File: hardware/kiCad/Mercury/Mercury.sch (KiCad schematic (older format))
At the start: 55 parts

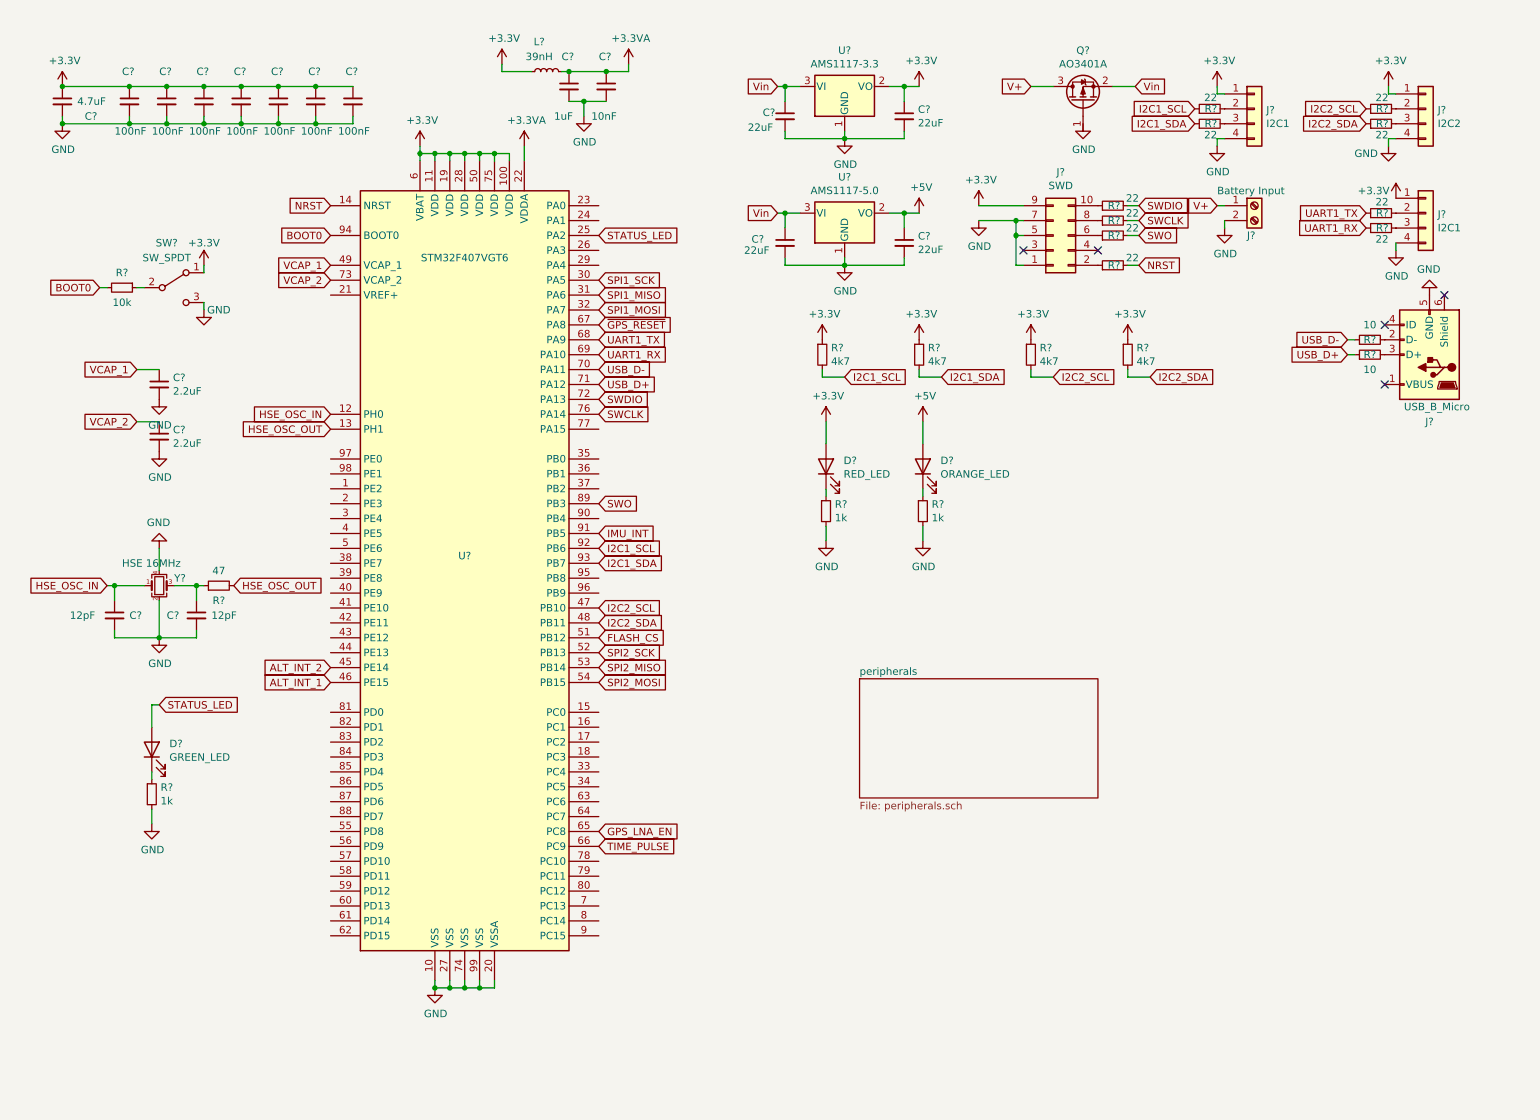
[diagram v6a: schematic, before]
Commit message: Schematic (Minus Connectors) Complete
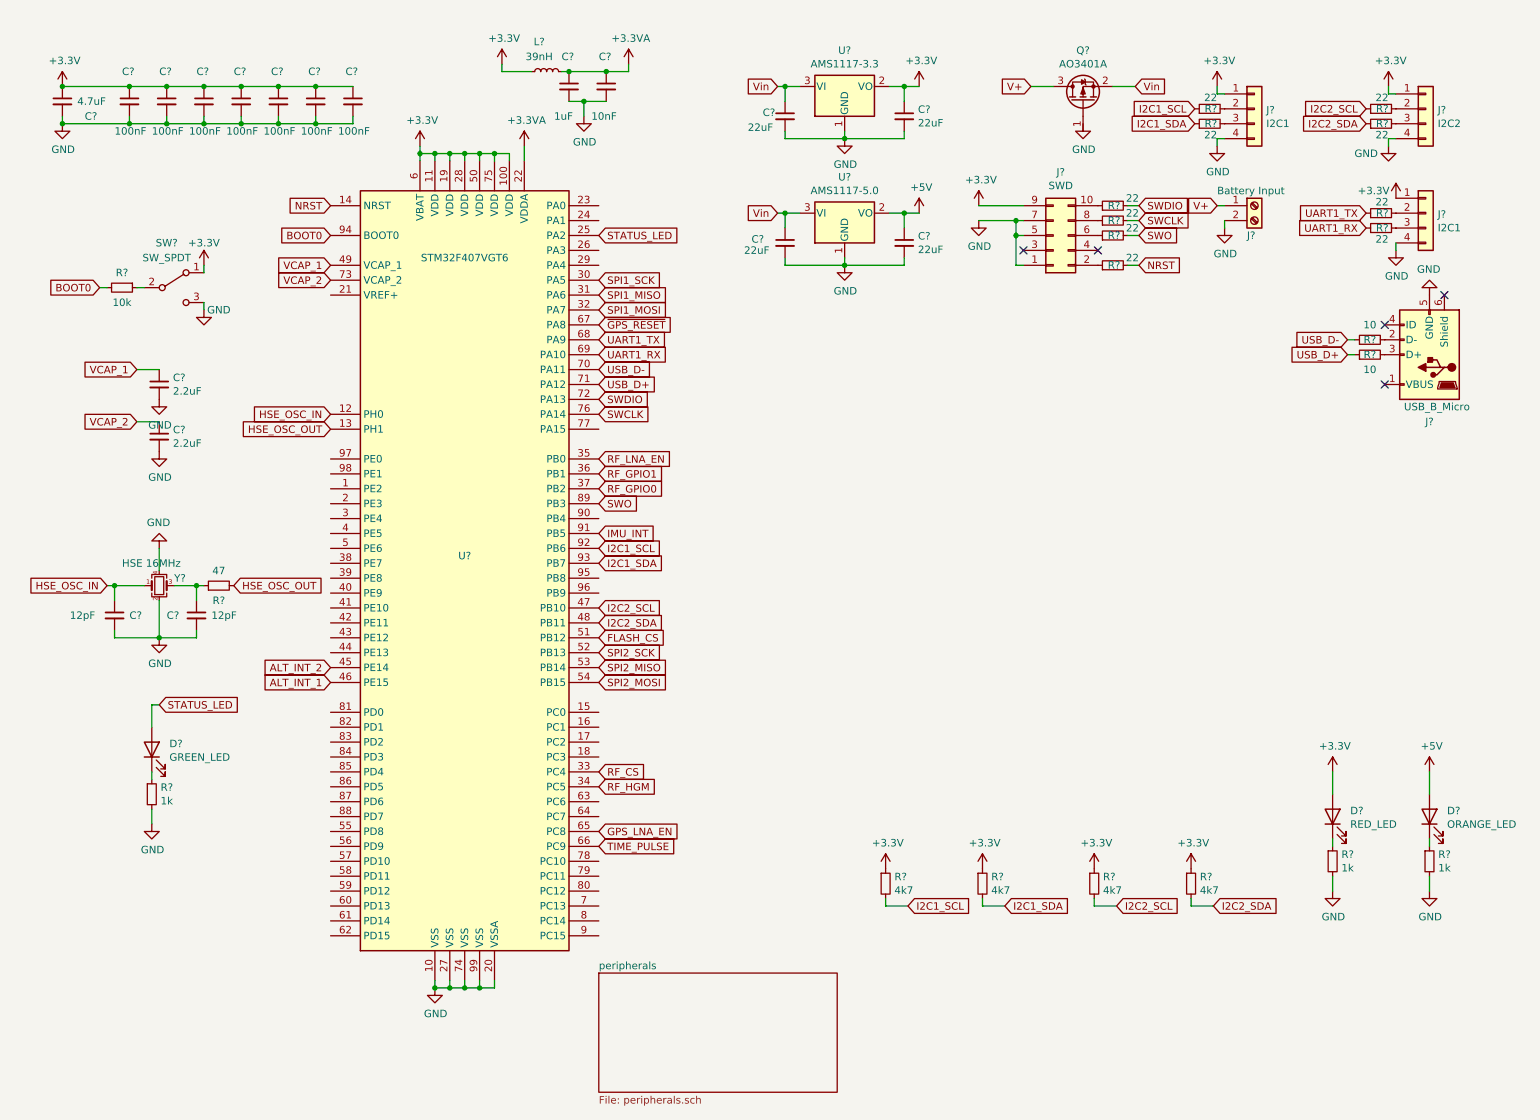
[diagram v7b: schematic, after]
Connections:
- net RF_CS: now reaches U?.33 (PC4)
- net RF_HGM: now reaches U?.34 (PC5)
- net RF_LNA_EN: now reaches U?.35 (PB0)
- net RF_GPIO1: now reaches U?.36 (PB1)
- net RF_GPIO0: now reaches U?.37 (PB2)
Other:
- moved on the sheet: D?, R?
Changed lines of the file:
@@
 	7100 2200 7150 2200
 Connection ~ 7100 2000
-Text GLabel 5950 2950 2    50   Input ~ 0
+Text GLabel 6375 6500 2    50   Input ~ 0
 I2C1_SCL
-Text GLabel 6600 2950 2    50   Input ~ 0
+Text GLabel 7025 6500 2    50   Input ~ 0
 I2C1_SDA
-Text GLabel 7350 2950 2    50   Input ~ 0
+Text GLabel 7775 6500 2    50   Input ~ 0
 I2C2_SCL
 $Comp
 L Device:R_Small R?
 U 1 1 5FED7803
-P 5800 2800
-F 0 "R?" H 5859 2846 50  0000 L CNN
-F 1 "4k7" H 5859 2755 50  0000 L CNN
-F 2 "" H 5800 2800 50  0001 C CNN
-F 3 "~" H 5800 2800 50  0001 C CNN
-	1    5800 2800
+P 6225 6350
+F 0 "R?" H 6284 6396 50  0000 L CNN
+F 1 "4k7" H 6284 6305 50  0000 L CNN
+F 2 "" H 6225 6350 50  0001 C CNN
+F 3 "~" H 6225 6350 50  0001 C CNN
+	1    6225 6350
 	1    0    0    -1
 $EndComp
@@
 L power:+3.3V #PWR?
 U 1 1 5FED8854
-P 5800 2700
-F 0 "#PWR?" H 5800 2550 50  0001 C CNN
-F 1 "+3.3V" H 5815 2873 50  0000 C CNN
-F 2 "" H 5800 2700 50  0001 C CNN
-F 3 "" H 5800 2700 50  0001 C CNN
-	1    5800 2700
-	1    0    0    -1
-$EndComp
-Wire Wire Line
-	5800 2900 5800 2950
-Wire Wire Line
-	5800 2950 5950 2950
+P 6225 6250
+F 0 "#PWR?" H 6225 6100 50  0001 C CNN
+F 1 "+3.3V" H 6240 6423 50  0000 C CNN
+F 2 "" H 6225 6250 50  0001 C CNN
+F 3 "" H 6225 6250 50  0001 C CNN
+	1    6225 6250
+	1    0    0    -1
+$EndComp
+Wire Wire Line
+	6225 6450 6225 6500
+Wire Wire Line
+	6225 6500 6375 6500
 $Comp
 L Device:R_Small R?
 U 1 1 5FEE7AE7
-P 6450 2800
-F 0 "R?" H 6509 2846 50  0000 L CNN
-F 1 "4k7" H 6509 2755 50  0000 L CNN
-F 2 "" H 6450 2800 50  0001 C CNN
-F 3 "~" H 6450 2800 50  0001 C CNN
-	1    6450 2800
+P 6875 6350
+F 0 "R?" H 6934 6396 50  0000 L CNN
+F 1 "4k7" H 6934 6305 50  0000 L CNN
+F 2 "" H 6875 6350 50  0001 C CNN
+F 3 "~" H 6875 6350 50  0001 C CNN
+	1    6875 6350
 	1    0    0    -1
 $EndComp
@@
 L power:+3.3V #PWR?
 U 1 1 5FEE7AED
-P 6450 2700
-F 0 "#PWR?" H 6450 2550 50  0001 C CNN
-F 1 "+3.3V" H 6465 2873 50  0000 C CNN
-F 2 "" H 6450 2700 50  0001 C CNN
-F 3 "" H 6450 2700 50  0001 C CNN
-	1    6450 2700
-	1    0    0    -1
-$EndComp
-Wire Wire Line
-	6450 2900 6450 2950
-Wire Wire Line
-	6450 2950 6600 2950
+P 6875 6250
+F 0 "#PWR?" H 6875 6100 50  0001 C CNN
+F 1 "+3.3V" H 6890 6423 50  0000 C CNN
+F 2 "" H 6875 6250 50  0001 C CNN
+F 3 "" H 6875 6250 50  0001 C CNN
+	1    6875 6250
+	1    0    0    -1
+$EndComp
+Wire Wire Line
+	6875 6450 6875 6500
+Wire Wire Line
+	6875 6500 7025 6500
 $Comp
 L Device:R_Small R?
 U 1 1 5FEED847
-P 7200 2800
-F 0 "R?" H 7259 2846 50  0000 L CNN
-F 1 "4k7" H 7259 2755 50  0000 L CNN
-F 2 "" H 7200 2800 50  0001 C CNN
-F 3 "~" H 7200 2800 50  0001 C CNN
-	1    7200 2800
+P 7625 6350
+F 0 "R?" H 7684 6396 50  0000 L CNN
+F 1 "4k7" H 7684 6305 50  0000 L CNN
+F 2 "" H 7625 6350 50  0001 C CNN
+F 3 "~" H 7625 6350 50  0001 C CNN
+	1    7625 6350
 	1    0    0    -1
 $EndComp
@@
 L power:+3.3V #PWR?
 U 1 1 5FEED84D
-P 7200 2700
-F 0 "#PWR?" H 7200 2550 50  0001 C CNN
-F 1 "+3.3V" H 7215 2873 50  0000 C CNN
-F 2 "" H 7200 2700 50  0001 C CNN
-F 3 "" H 7200 2700 50  0001 C CNN
-	1    7200 2700
-	1    0    0    -1
-$EndComp
-Wire Wire Line
-	7200 2900 7200 2950
-Wire Wire Line
-	7200 2950 7350 2950
+P 7625 6250
+F 0 "#PWR?" H 7625 6100 50  0001 C CNN
+F 1 "+3.3V" H 7640 6423 50  0000 C CNN
+F 2 "" H 7625 6250 50  0001 C CNN
+F 3 "" H 7625 6250 50  0001 C CNN
+	1    7625 6250
+	1    0    0    -1
+$EndComp
+Wire Wire Line
+	7625 6450 7625 6500
+Wire Wire Line
+	7625 6500 7775 6500
 $Comp
 L Device:R_Small R?
 U 1 1 5FEF1716
-P 7850 2800
-F 0 "R?" H 7909 2846 50  0000 L CNN
-F 1 "4k7" H 7909 2755 50  0000 L CNN
-F 2 "" H 7850 2800 50  0001 C CNN
-F 3 "~" H 7850 2800 50  0001 C CNN
-	1    7850 2800
+P 8275 6350
+F 0 "R?" H 8334 6396 50  0000 L CNN
+F 1 "4k7" H 8334 6305 50  0000 L CNN
+F 2 "" H 8275 6350 50  0001 C CNN
+F 3 "~" H 8275 6350 50  0001 C CNN
+	1    8275 6350
 	1    0    0    -1
 $EndComp
@@
 L power:+3.3V #PWR?
 U 1 1 5FEF171C
-P 7850 2700
-F 0 "#PWR?" H 7850 2550 50  0001 C CNN
-F 1 "+3.3V" H 7865 2873 50  0000 C CNN
-F 2 "" H 7850 2700 50  0001 C CNN
-F 3 "" H 7850 2700 50  0001 C CNN
-	1    7850 2700
-	1    0    0    -1
-$EndComp
-Wire Wire Line
-	7850 2900 7850 2950
-Wire Wire Line
-	7850 2950 8000 2950
+P 8275 6250
+F 0 "#PWR?" H 8275 6100 50  0001 C CNN
+F 1 "+3.3V" H 8290 6423 50  0000 C CNN
+F 2 "" H 8275 6250 50  0001 C CNN
+F 3 "" H 8275 6250 50  0001 C CNN
+	1    8275 6250
+	1    0    0    -1
+$EndComp
+Wire Wire Line
+	8275 6450 8275 6500
+Wire Wire Line
+	8275 6500 8425 6500
 Wire Wire Line
 	5500 1000 5550 1000
@@
 	0    -1   -1   0
 $EndComp
-Text GLabel 8000 2950 2    50   Input ~ 0
+Text GLabel 8425 6500 2    50   Input ~ 0
 I2C2_SDA
 Text GLabel 9450 1250 0    50   Input ~ 0
@@
 L Device:LED D?
 U 1 1 5FF00635
-P 5825 3550
-F 0 "D?" V 5864 3432 50  0000 R CNN
-F 1 "RED_LED" V 5773 3432 50  0000 R CNN
-F 2 "" H 5825 3550 50  0001 C CNN
-F 3 "~" H 5825 3550 50  0001 C CNN
-	1    5825 3550
-	0    -1   -1   0
-$EndComp
-Wire Wire Line
-	5825 3400 5825 3250
+P 9225 5900
+F 0 "D?" V 9264 5782 50  0000 R CNN
+F 1 "RED_LED" V 9173 5782 50  0000 R CNN
+F 2 "" H 9225 5900 50  0001 C CNN
+F 3 "~" H 9225 5900 50  0001 C CNN
+	1    9225 5900
+	0    -1   -1   0
+$EndComp
+Wire Wire Line
+	9225 5750 9225 5600
 $Comp
 L power:GND #PWR?
 U 1 1 5FF0063D
-P 5825 4050
-F 0 "#PWR?" H 5825 3800 50  0001 C CNN
-F 1 "GND" H 5830 3877 50  0000 C CNN
-F 2 "" H 5825 4050 50  0001 C CNN
-F 3 "" H 5825 4050 50  0001 C CNN
-	1    5825 4050
+P 9225 6400
+F 0 "#PWR?" H 9225 6150 50  0001 C CNN
+F 1 "GND" H 9230 6227 50  0000 C CNN
+F 2 "" H 9225 6400 50  0001 C CNN
+F 3 "" H 9225 6400 50  0001 C CNN
+	1    9225 6400
 	1    0    0    -1
 $EndComp
@@
 L Device:R_Small R?
 U 1 1 5FF00643
-P 5825 3850
-F 0 "R?" H 5884 3896 50  0000 L CNN
-F 1 "1k" H 5884 3805 50  0000 L CNN
-F 2 "" H 5825 3850 50  0001 C CNN
-F 3 "~" H 5825 3850 50  0001 C CNN
-	1    5825 3850
-	1    0    0    -1
-$EndComp
-Wire Wire Line
-	5825 3950 5825 4050
-Wire Wire Line
-	5825 3700 5825 3750
+P 9225 6200
+F 0 "R?" H 9284 6246 50  0000 L CNN
+F 1 "1k" H 9284 6155 50  0000 L CNN
+F 2 "" H 9225 6200 50  0001 C CNN
+F 3 "~" H 9225 6200 50  0001 C CNN
+	1    9225 6200
+	1    0    0    -1
+$EndComp
+Wire Wire Line
+	9225 6300 9225 6400
+Wire Wire Line
+	9225 6050 9225 6100
 $Comp
 L power:+3.3V #PWR?
 U 1 1 5FF04D6A
-P 5825 3250
-F 0 "#PWR?" H 5825 3100 50  0001 C CNN
-F 1 "+3.3V" H 5840 3423 50  0000 C CNN
-F 2 "" H 5825 3250 50  0001 C CNN
-F 3 "" H 5825 3250 50  0001 C CNN
-	1    5825 3250
+P 9225 5600
+F 0 "#PWR?" H 9225 5450 50  0001 C CNN
+F 1 "+3.3V" H 9240 5773 50  0000 C CNN
+F 2 "" H 9225 5600 50  0001 C CNN
+F 3 "" H 9225 5600 50  0001 C CNN
+	1    9225 5600
 	1    0    0    -1
 $EndComp
@@
 L Device:LED D?
 U 1 1 5FF102DA
-P 6475 3550
-F 0 "D?" V 6514 3432 50  0000 R CNN
-F 1 "ORANGE_LED" V 6423 3432 50  0000 R CNN
-F 2 "" H 6475 3550 50  0001 C CNN
-F 3 "~" H 6475 3550 50  0001 C CNN
-	1    6475 3550
-	0    -1   -1   0
-$EndComp
-Wire Wire Line
-	6475 3400 6475 3250
+P 9875 5900
+F 0 "D?" V 9914 5782 50  0000 R CNN
+F 1 "ORANGE_LED" V 9823 5782 50  0000 R CNN
+F 2 "" H 9875 5900 50  0001 C CNN
+F 3 "~" H 9875 5900 50  0001 C CNN
+	1    9875 5900
+	0    -1   -1   0
+$EndComp
+Wire Wire Line
+	9875 5750 9875 5600
 $Comp
 L power:GND #PWR?
 U 1 1 5FF10A7F
-P 6475 4050
-F 0 "#PWR?" H 6475 3800 50  0001 C CNN
-F 1 "GND" H 6480 3877 50  0000 C CNN
-F 2 "" H 6475 4050 50  0001 C CNN
-F 3 "" H 6475 4050 50  0001 C CNN
-	1    6475 4050
+P 9875 6400
+F 0 "#PWR?" H 9875 6150 50  0001 C CNN
+F 1 "GND" H 9880 6227 50  0000 C CNN
+F 2 "" H 9875 6400 50  0001 C CNN
+F 3 "" H 9875 6400 50  0001 C CNN
+	1    9875 6400
 	1    0    0    -1
 $EndComp
@@
 L Device:R_Small R?
 U 1 1 5FF10A89
-P 6475 3850
-F 0 "R?" H 6534 3896 50  0000 L CNN
-F 1 "1k" H 6534 3805 50  0000 L CNN
-F 2 "" H 6475 3850 50  0001 C CNN
-F 3 "~" H 6475 3850 50  0001 C CNN
-	1    6475 3850
-	1    0    0    -1
-$EndComp
-Wire Wire Line
-	6475 3950 6475 4050
-Wire Wire Line
-	6475 3700 6475 3750
+P 9875 6200
+F 0 "R?" H 9934 6246 50  0000 L CNN
+F 1 "1k" H 9934 6155 50  0000 L CNN
+F 2 "" H 9875 6200 50  0001 C CNN
+F 3 "~" H 9875 6200 50  0001 C CNN
+	1    9875 6200
+	1    0    0    -1
+$EndComp
+Wire Wire Line
+	9875 6300 9875 6400
+Wire Wire Line
+	9875 6050 9875 6100
 $Comp
 L power:+5V #PWR?
 U 1 1 5FF1B774
-P 6475 3250
-F 0 "#PWR?" H 6475 3100 50  0001 C CNN
-F 1 "+5V" H 6490 3423 50  0000 C CNN
-F 2 "" H 6475 3250 50  0001 C CNN
-F 3 "" H 6475 3250 50  0001 C CNN
-	1    6475 3250
+P 9875 5600
+F 0 "#PWR?" H 9875 5450 50  0001 C CNN
+F 1 "+5V" H 9890 5773 50  0000 C CNN
+F 2 "" H 9875 5600 50  0001 C CNN
+F 3 "" H 9875 5600 50  0001 C CNN
+	1    9875 5600
 	1    0    0    -1
 $EndComp
@@
 $EndComp
 $Sheet
-S 6050 4975 1600 800
+S 4300 6950 1600 800
 U 5FE81F4B
 F0 "peripherals" 50
@@
 Text GLabel 4300 6000 2    50   Input ~ 0
 GPS_LNA_EN
+Text GLabel 4300 5600 2    50   Input ~ 0
+RF_CS
+Text GLabel 4300 5700 2    50   Input ~ 0
+RF_HGM
+Text GLabel 4300 3500 2    50   Input ~ 0
+RF_LNA_EN
+Text GLabel 4300 3600 2    50   Input ~ 0
+RF_GPIO1
+Text GLabel 4300 3700 2    50   Input ~ 0
+RF_GPIO0
 $EndSCHEMATC
